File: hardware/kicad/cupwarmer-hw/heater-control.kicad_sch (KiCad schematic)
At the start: 6 parts, among them Q1 AO3400 SOT-23

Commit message: Align cupwarmer BOM with STEVAL-WLC38RX reference (JLCPCB-orderable)
- Pick concrete JLCPCB MPNs for all TBD parts in initial-bom.csv:
  - Cs (5x 100nF) and 100nF bypass roles → Wuerth 885012206095 (C6715111),
    matching STEVAL exactly.
  - 10uF rectifier/output bulk → Murata GRM188R6YA106MA73D (C194427).
  - 4.7uF VAA → Murata GRM188R61E475KE11D (C90057).
  - Add VRECT/VOUT bulk + HF + Z4 SMBJ18A clamp per STEVAL UM3154.
  - Other passives: Samsung MLCC, UNI-ROYAL 0603 1% resistors,
    KEXIN 10k NTC, SMF13A/SMBJ15A TVS, AO3400, KSD9700-70.
- Add `lcsc` column to BOM CSV; mark mechanical/board-feature rows.
- Sync MPN/LCSC/Manufacturer properties onto every schematic symbol via
  tmp/apply_bom_properties.py (idempotent helper).
- pcb_netlist.py: always seed fp-lib-table from stock template so system
  libraries resolve when the global table is just a Table-type indirection.
- design-notes: document VRECT/VOUT cap network and Z3/Z4 TVS choices.
- CLAUDE.md / wiki/README.md: point at ./wiki/ as the project's reference
  store.

Co-Authored-By: Claude Opus 4.7 (1M context) <noreply@anthropic.com>
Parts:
- F1: LCSC (none) -> C156512; MPN (none) -> KSD9700-70/5JSB/080C; Manufacturer (none) -> Xucheng Elec
- Q1: LCSC (none) -> C181090; MPN (none) -> AO3400; Manufacturer (none) -> Shenzhen Hottech Electronics
- R1, R2: LCSC (none) -> C25804; MPN (none) -> 0603WAF1002T5E; Manufacturer (none) -> UNI-ROYAL
- R3: LCSC (none) -> C21189; MPN (none) -> 0603WAF0000T5E; Manufacturer (none) -> UNI-ROYAL
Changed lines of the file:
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@@
+			)
+		)
+		(property "Manufacturer" "Xucheng Elec"
+			(at 0 0 0)
+			(hide yes)
+			(show_name no)
+			(do_not_autoplace no)
+			(effects
+				(font
+					(size 1.27 1.27)
+				)
+			)
+		)
+		(property "LCSC" "C156512"
+			(at 0 0 0)
+			(hide yes)
+			(show_name no)
+			(do_not_autoplace no)
+			(effects
+				(font
+					(size 1.27 1.27)
+				)
+			)
+		)
+		(property "MPN" "KSD9700-70/5JSB/080C"
+			(at 0 0 0)
+			(hide yes)
+			(show_name no)
+			(do_not_autoplace no)
+			(effects
+				(font
+					(size 1.27 1.27)
+				)
 			)
 		)
@@
 			)
 		)
+		(property "Manufacturer" "Shenzhen Hottech Electronics"
+			(at 0 0 0)
+			(hide yes)
+			(show_name no)
+			(do_not_autoplace no)
+			(effects
+				(font
+					(size 1.27 1.27)
+				)
+			)
+		)
+		(property "LCSC" "C181090"
+			(at 0 0 0)
+			(hide yes)
+			(show_name no)
+			(do_not_autoplace no)
+			(effects
+				(font
+					(size 1.27 1.27)
+				)
+			)
+		)
+		(property "MPN" "AO3400"
+			(at 0 0 0)
+			(hide yes)
+			(show_name no)
+			(do_not_autoplace no)
+			(effects
+				(font
+					(size 1.27 1.27)
+				)
+			)
+		)
 		(pin "1"
 		)
@@
 			)
 		)
+		(property "Manufacturer" "UNI-ROYAL"
+			(at 0 0 0)
+			(hide yes)
+			(show_name no)
+			(do_not_autoplace no)
+			(effects
+				(font
+					(size 1.27 1.27)
+				)
+			)
+		)
+		(property "LCSC" "C25804"
+			(at 0 0 0)
+			(hide yes)
+			(show_name no)
+			(do_not_autoplace no)
+			(effects
+				(font
+					(size 1.27 1.27)
+				)
+			)
+		)
+		(property "MPN" "0603WAF1002T5E"
+			(at 0 0 0)
+			(hide yes)
+			(show_name no)
+			(do_not_autoplace no)
+			(effects
+				(font
+					(size 1.27 1.27)
+				)
+			)
+		)
 		(pin "1"
 		)
@@
 			)
 		)
+		(property "Manufacturer" "UNI-ROYAL"
+			(at 0 0 0)
+			(hide yes)
+			(show_name no)
+			(do_not_autoplace no)
+			(effects
+				(font
+					(size 1.27 1.27)
+				)
+			)
+		)
+		(property "LCSC" "C25804"
+			(at 0 0 0)
+			(hide yes)
+			(show_name no)
+			(do_not_autoplace no)
+			(effects
+				(font
+					(size 1.27 1.27)
+				)
+			)
+		)
+		(property "MPN" "0603WAF1002T5E"
+			(at 0 0 0)
+			(hide yes)
+			(show_name no)
+			(do_not_autoplace no)
+			(effects
+				(font
+					(size 1.27 1.27)
+				)
+			)
+		)
 		(pin "1"
 		)
@@
 			(hide yes)
 			(show_name no)
+			(do_not_autoplace no)
+			(effects
+				(font
+					(size 1.27 1.27)
+				)
+			)
+		)
+		(property "Manufacturer" "UNI-ROYAL"
+			(at 0 0 0)
+			(hide yes)
+			(show_name no)
+			(do_not_autoplace no)
+			(effects
+				(font
+					(size 1.27 1.27)
+				)
+			)
+		)
+		(property "LCSC" "C21189"
+			(at 0 0 0)
+			(hide yes)
+			(show_name no)
+			(do_not_autoplace no)
+			(effects
+				(font
+					(size 1.27 1.27)
+				)
+			)
+		)
+		(property "MPN" "0603WAF0000T5E"
+			(at 0 0 0)
+			(hide yes)
+			(show_name no)

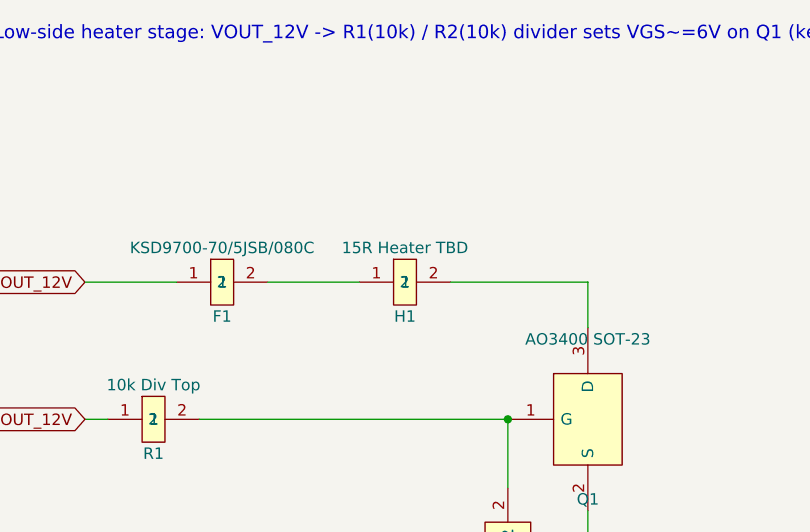
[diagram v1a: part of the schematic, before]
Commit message: Apply ST UM3154 review fixes to Qi RX schematic
Address tape-out blockers from STEVAL-WLC38RX (UM3154) reference diff:

- Add R12 (10k) INTB pullup to RX_VAA on rx-power
- Add R13 (10k) ENB pulldown to SYS_GND on rx-power
  (replaces direct ENB->GND tie; matches ST eval, allows future MCU control)
- C18, C19 value 100nF -> 10nF (NP0) on rx-power
  (Cs=320nF total with 8uH coil targets ~99.5kHz Qi resonance vs prior 79.6kHz)
- Replace TH2 with Murata NCP18WF104F12RB 100k B25/85=4260K on sensors-logic
  (matches ST eval reference 100k NTC; aligns with default HOTP threshold)
- Remove TH1 + R8 + J2 (THERM_MON) and NTC_TOP labels from sensors-logic
  (redundant; KSD9700 + STWLC38 HOTP via TH2 already provide thermal protection)
- BOM: add R12, R13; replace TH2 entry; split C1/16/17/18/19 into two rows;
  drop TH1, R8, J2; tweak R7 description
- heater-control: H1 Value text updated to "12R 12W Heater (external)"

ERC: 0 errors, 0 warnings.

Co-Authored-By: Claude Opus 4.7 (1M context) <noreply@anthropic.com>
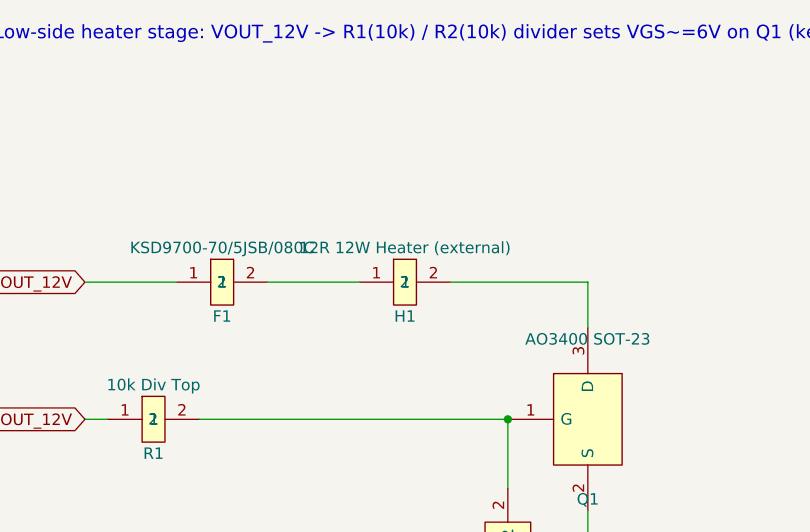
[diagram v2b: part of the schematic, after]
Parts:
- H1: value 15R Heater TBD -> 12R 12W Heater (external)
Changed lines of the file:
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@@
 			)
 		)
-		(property "Value" "15R Heater TBD"
+		(property "Value" "12R 12W Heater (external)"
 			(at 76.2 54.61 0)
 			(show_name no)

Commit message: Switch L1/F1/H1 to no-relief SolderWire footprints
Relief / Relief2x variants extend 13.8-27.6mm of strain-relief tail
that conflicts with adjacent courtyards on the phi76mm board. For
hand-soldering with enclosure-side wire fixation, plain 2-pad THT is
sufficient.

- sch (rx-power, heater-control): drop _Relief2x / _Relief suffix from
  L1, F1, H1 Footprint properties
- pcb: re-import the three footprints from sch and reposition
  (L1 130,88 rot=90; F1 128,108; H1 122,120) to clear edge clearance
  and silk overlaps
- BOM: L1 / F1 notes updated to reflect no-relief land + enclosure
  strain-relief assumption

DRC: 195 -> 171 violations; no functional errors on L1/F1/H1 (only
benign lib_footprint_mismatch warnings).

Co-Authored-By: Claude Opus 4.7 (1M context) <noreply@anthropic.com>
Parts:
- F1: footprint Connector_Wire:SolderWire-0.5sqmm_1x02_P4.8mm_D0.9mm_OD2.3mm_Relief2x -> Connector_Wire:SolderWire-0.5sqmm_1x02_P4.8mm_D0.9mm_OD2.3mm
- H1: footprint Connector_Wire:SolderWire-1sqmm_1x02_P5.4mm_D1.4mm_OD2.7mm_Relief -> Connector_Wire:SolderWire-1sqmm_1x02_P5.4mm_D1.4mm_OD2.7mm
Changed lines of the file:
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@@
 			)
 		)
-		(property "Footprint" "Connector_Wire:SolderWire-0.5sqmm_1x02_P4.8mm_D0.9mm_OD2.3mm_Relief2x"
+		(property "Footprint" "Connector_Wire:SolderWire-0.5sqmm_1x02_P4.8mm_D0.9mm_OD2.3mm"
 			(at 55.88 58.42 0)
 			(hide yes)
@@
 			)
 		)
-		(property "Footprint" "Connector_Wire:SolderWire-1sqmm_1x02_P5.4mm_D1.4mm_OD2.7mm_Relief"
+		(property "Footprint" "Connector_Wire:SolderWire-1sqmm_1x02_P5.4mm_D1.4mm_OD2.7mm"
 			(at 76.2 58.42 0)
 			(hide yes)

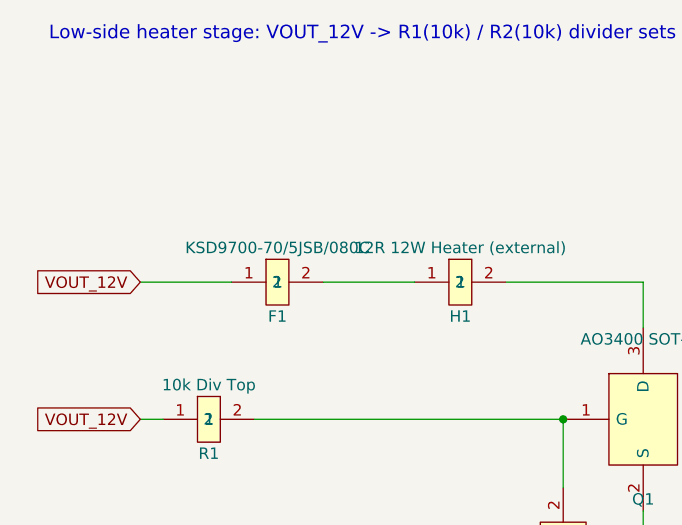
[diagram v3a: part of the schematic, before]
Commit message: Pour SYS_GND on inner layers and label rx-power nets
- PCB: add SYS_GND zones on In1.Cu/In2.Cu, add GND stitching vias,
  reflow footprint placement
- rx-power.sch: label AC1/2, COMA1/2, COMB1/2, BOOT1/2, VRECT nets
- heater-control.sch: nudge KSD9700 value label
- project: housekeeping from KiCad open

Co-Authored-By: Claude Opus 4.7 (1M context) <noreply@anthropic.com>
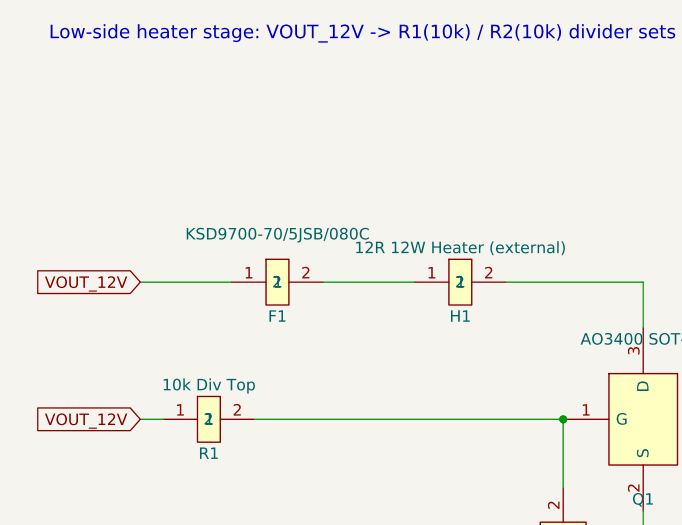
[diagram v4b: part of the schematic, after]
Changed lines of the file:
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@@
 		)
 		(property "Value" "KSD9700-70/5JSB/080C"
-			(at 55.88 54.61 0)
+			(at 55.88 53.086 0)
 			(show_name no)
 			(do_not_autoplace no)

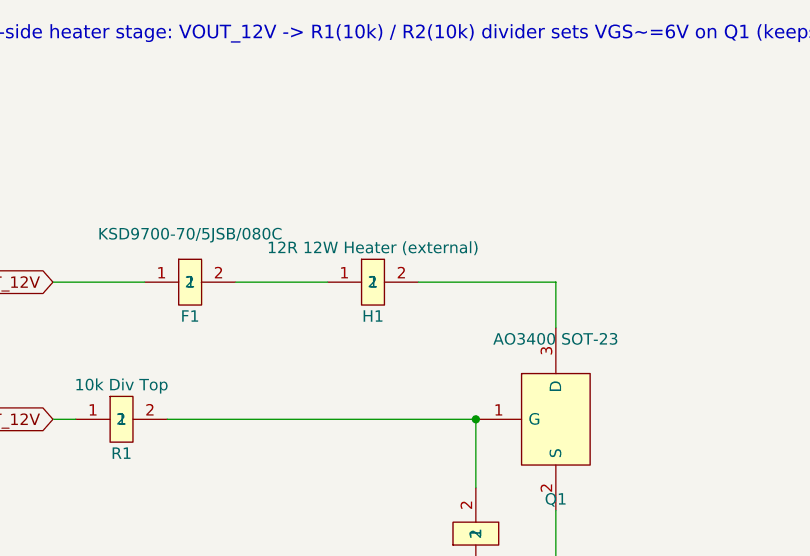
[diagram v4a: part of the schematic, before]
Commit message: Tag HEATER_IN/OUT as POWER and refresh DRC exclusions
Add HEATER_IN/HEATER_OUT labels in heater-control and assign them to
the POWER netclass. Refresh hole_to_hole DRC exclusions after the
recent PCB rework.

Co-Authored-By: Claude Opus 4.7 (1M context) <noreply@anthropic.com>
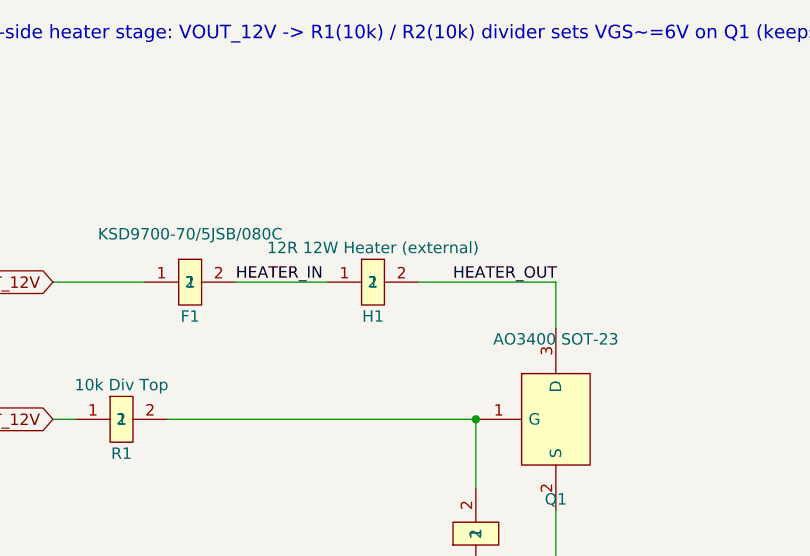
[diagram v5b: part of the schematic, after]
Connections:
- net HEATER_IN: now reaches F1.2, H1.1
- net HEATER_OUT: now reaches H1.2, Q1.3 (D)
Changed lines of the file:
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@@
+		)
+	)
+	(label "HEATER_OUT"
+		(at 85.09 58.42 0)
+		(effects
+			(font
+				(size 1.27 1.27)
+			)
+			(justify left bottom)
+		)
+	)
+	(label "HEATER_IN"
+		(at 60.96 58.42 0)
+		(effects
+			(font
+				(size 1.27 1.27)
+			)
+			(justify left bottom)
 		)
 	)
